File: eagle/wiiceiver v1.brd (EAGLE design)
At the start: 35.2 x 50.8 mm, 16 parts, among them IC1 ATmega328P

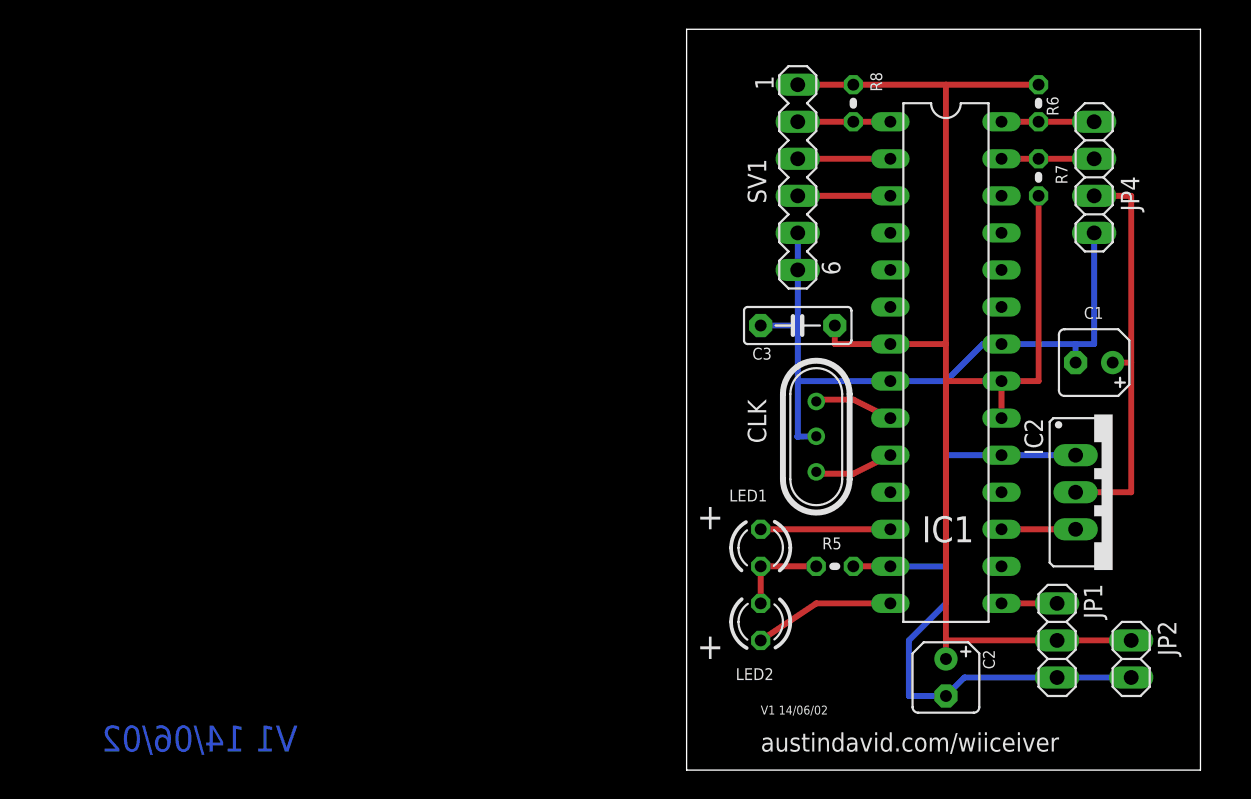
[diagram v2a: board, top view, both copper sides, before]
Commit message: minor update for calibration function
calibrates in 1s now, and more reliably

also some minor changes to the schematic, fixing glitches
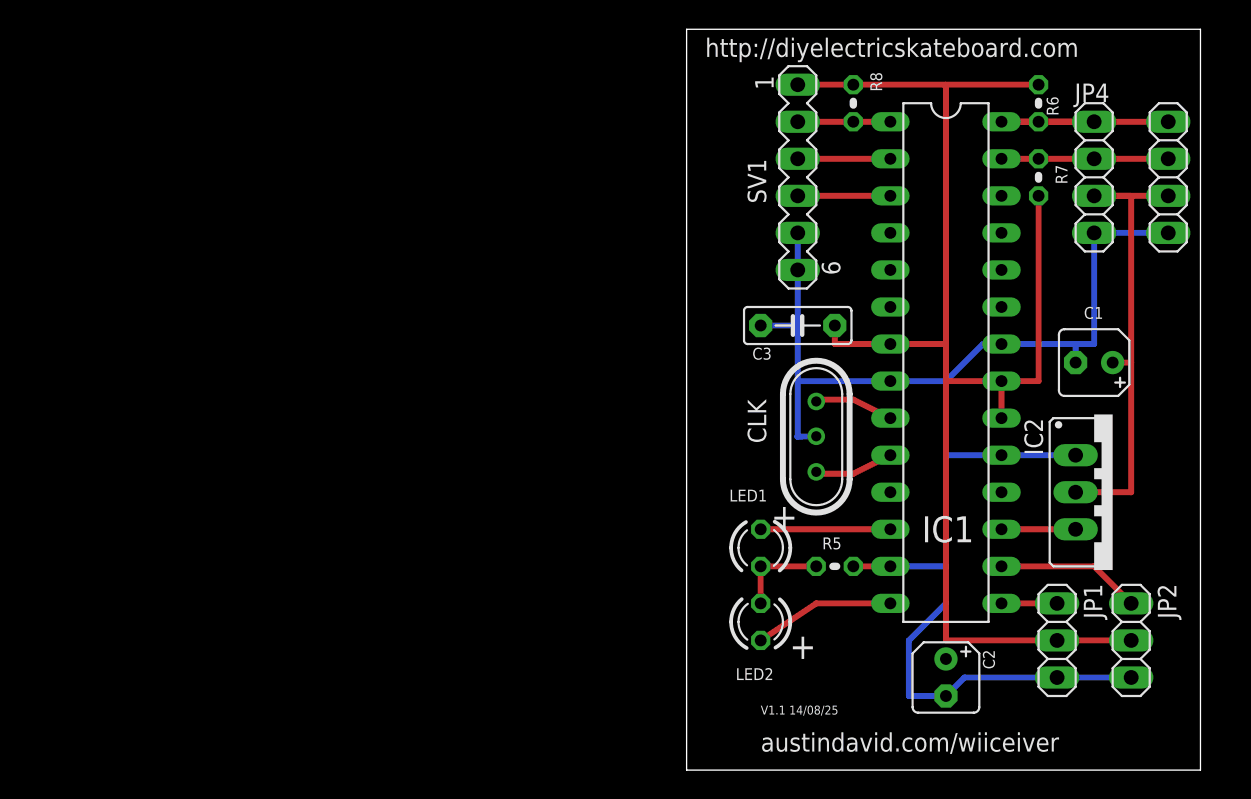
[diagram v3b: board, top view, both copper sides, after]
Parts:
- added JP3: (no value), pinhead:1X04
- JP2: device pinhead:1X02 -> pinhead:1X03
- moved JP2 1.27 mm to (52.1, 30.5)
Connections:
- new net N$3: IC1.26
- new net N$4: IC1.16, JP2.1
- net GND: now also C2.+, JP2.3, JP3.4, R6.2, R7.2, R8.1, SV1.1; no longer JP2.2
- net N$16: now also JP3.2, JP3.3
- net N$21: now also JP3.1
- net VIN: now also JP2.2; no longer C2.+, JP2.1, R6.2, R7.2, R8.1, SV1.1
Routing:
- net GND: track 101.7 -> 136.0 mm
- net VIN: track 99.1 -> 68.6 mm
- net N$21: track 6.35 -> 17.8 mm
- net N$16: track 27.9 -> 38.1 mm
- net N$4: track 0.00 -> 9.94 mm
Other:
- board text added: "V1.1 14/08/25"
- board text added: "http://diyelectricskateboard.com"
- board text removed: "V1 14/06/02"
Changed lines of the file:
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@@
 <setting verticaltext="up"/>
 </settings>
-<grid distance="0.05" unitdist="inch" unit="inch" style="lines" multiple="1" display="yes" altdistance="0.025" altunitdist="inch" altunit="inch"/>
+<grid distance="0.025" unitdist="inch" unit="inch" style="lines" multiple="1" display="yes" altdistance="0.025" altunitdist="inch" altunit="inch"/>
 <layers>
 <layer number="1" name="Top" color="4" fill="1" visible="yes" active="yes"/>
@@
 <wire x1="21.59" y1="72.38" x2="21.59" y2="21.59" width="0" layer="20"/>
 <text x="26.67" y="22.86" size="1.27" layer="25">austindavid.com/wiiceiver</text>
-<text x="24.13" y="29.21" size="1.778" layer="25" rot="MR0">+</text>
-<text x="24.13" y="38.1" size="1.778" layer="25" rot="MR0">+</text>
-<text x="-5.08" y="22.86" size="1.778" layer="16" rot="MR0">V1 14/06/02</text>
-<text x="26.67" y="25.4" size="0.6096" layer="25">V1 14/06/02</text>
+<text x="30.48" y="29.21" size="1.778" layer="25" rot="MR0">+</text>
+<text x="29.21" y="38.1" size="1.778" layer="25" rot="MR0">+</text>
+<text x="26.67" y="25.4" size="0.6096" layer="25">V1.1 14/08/25</text>
+<text x="22.86" y="70.485" size="1.27" layer="25">http://diyelectricskateboard.com</text>
 </plain>
 <attributes>
@@
 </element>
 <element name="JP1" library="pinhead" package="1X03" value="Servo" x="46.99" y="30.48" rot="R270"/>
-<element name="JP2" library="pinhead" package="1X02" value="BEC" x="52.07" y="29.21" rot="R270"/>
+<element name="JP2" library="pinhead" package="1X03" value="BEC" x="52.07" y="30.48" rot="R270"/>
 <element name="CLK" library="crystal" package="HC49U" value="16MHz" x="30.48" y="44.45" smashed="yes" rot="R270">
 <attribute name="OC_NEWARK" value="unknown" x="-11.43" y="25.4" size="1.778" layer="27" rot="R270" display="off"/>
@@
 </element>
 <element name="JP4" library="pinhead" package="1X04" value="Nunchuck Hole" x="49.53" y="62.23" smashed="yes" rot="R270">
-<attribute name="NAME" x="51.3588" y="62.3062" size="1.27" layer="25" ratio="10" rot="R270"/>
+<attribute name="NAME" x="48.1838" y="67.3862" size="1.27" layer="25" ratio="10"/>
 <attribute name="VALUE" x="46.355" y="67.31" size="1.27" layer="27" rot="R270"/>
 </element>
@@
 <attribute name="NAME" x="25.781" y="63.5" size="1.27" layer="25" ratio="10" rot="R270"/>
 <attribute name="VALUE" x="26.289" y="64.77" size="1.27" layer="27" ratio="10" rot="R270"/>
+</element>
+<element name="JP3" library="pinhead" package="1X04" value="" x="54.61" y="62.23" smashed="yes" rot="R270">
+<attribute name="VALUE" x="51.435" y="67.31" size="1.27" layer="27" rot="R270"/>
 </element>
 </elements>
@@
 <contactref element="IC2" pad="2"/>
 <wire x1="48.26" y1="40.64" x2="52.07" y2="40.64" width="0.4064" layer="1"/>
+<contactref element="JP3" pad="3"/>
+<contactref element="JP3" pad="2"/>
+<wire x1="54.61" y1="63.5" x2="49.53" y2="63.5" width="0.4064" layer="1"/>
+<wire x1="49.53" y1="60.96" x2="54.61" y2="60.96" width="0.4064" layer="1"/>
+<wire x1="54.61" y1="60.96" x2="54.61" y2="63.5" width="0" layer="19" extent="1-1"/>
 </signal>
 <signal name="N$21">
@@
 <wire x1="43.18" y1="66.04" x2="45.72" y2="66.04" width="0.4064" layer="1"/>
 <wire x1="45.72" y1="66.04" x2="49.53" y2="66.04" width="0.4064" layer="1"/>
+<contactref element="JP3" pad="1"/>
+<wire x1="43.18" y1="66.04" x2="49.53" y2="66.04" width="0.4064" layer="1"/>
+<wire x1="49.53" y1="66.04" x2="54.61" y2="66.04" width="0.4064" layer="1"/>
 </signal>
 <signal name="N$22">
@@
 <contactref element="R5" pad="2"/>
 <contactref element="JP4" pad="4"/>
-<contactref element="JP2" pad="2"/>
-<contactref element="JP1" pad="3"/>
 <contactref element="C2" pad="-"/>
 <contactref element="IC1" pad="22"/>
@@
 <wire x1="43.18" y1="50.8" x2="48.26" y2="50.8" width="0.4064" layer="16"/>
 <wire x1="48.26" y1="50.8" x2="49.53" y2="50.8" width="0.4064" layer="16"/>
-<wire x1="52.07" y1="27.94" x2="46.99" y2="27.94" width="0.4064" layer="16"/>
 <wire x1="26.67" y1="52.07" x2="29.21" y2="52.07" width="0.4064" layer="16"/>
 <wire x1="29.21" y1="44.45" x2="29.21" y2="48.26" width="0.4064" layer="16"/>
@@
 <wire x1="49.53" y1="58.42" x2="49.53" y2="50.8" width="0.4064" layer="16"/>
 <wire x1="48.26" y1="49.53" x2="48.26" y2="50.8" width="0.4064" layer="16"/>
-<wire x1="46.99" y1="27.94" x2="40.64" y2="27.94" width="0.4064" layer="16"/>
 <wire x1="40.64" y1="27.94" x2="39.37" y2="26.67" width="0.4064" layer="16"/>
 <wire x1="39.37" y1="35.56" x2="39.37" y2="33.02" width="0.4064" layer="16"/>
@@
 <wire x1="29.21" y1="58.42" x2="29.21" y2="55.88" width="0.4064" layer="16"/>
 <wire x1="29.21" y1="55.88" x2="29.21" y2="52.07" width="0.4064" layer="16"/>
+<contactref element="C2" pad="+"/>
+<contactref element="R7" pad="2"/>
+<contactref element="R6" pad="2"/>
+<contactref element="R8" pad="1"/>
+<contactref element="SV1" pad="1"/>
+<contactref element="JP1" pad="3"/>
+<wire x1="33.02" y1="68.58" x2="29.21" y2="68.58" width="0.4064" layer="1"/>
+<contactref element="JP2" pad="3"/>
+<wire x1="52.07" y1="27.94" x2="46.99" y2="27.94" width="0.4064" layer="16"/>
+<wire x1="46.99" y1="27.94" x2="40.64" y2="27.94" width="0.4064" layer="16"/>
+<wire x1="33.02" y1="68.58" x2="45.72" y2="68.58" width="0.4064" layer="1"/>
+<wire x1="45.72" y1="60.96" x2="45.72" y2="48.26" width="0.4064" layer="1"/>
+<contactref element="JP3" pad="4"/>
+<wire x1="54.61" y1="58.42" x2="49.53" y2="58.42" width="0.4064" layer="16"/>
+<wire x1="45.72" y1="60.96" x2="45.72" y2="68.58" width="0" layer="19" extent="1-1"/>
+<wire x1="48.26" y1="49.53" x2="45.72" y2="48.26" width="0" layer="19" extent="1-1"/>
+<wire x1="39.37" y1="29.21" x2="40.64" y2="27.94" width="0" layer="19" extent="16-16"/>
 </signal>
 <signal name="VIN">
-<contactref element="JP2" pad="1"/>
 <contactref element="JP1" pad="2"/>
 <contactref element="IC1" pad="21"/>
@@
 <contactref element="IC1" pad="7"/>
 <contactref element="C3" pad="1"/>
-<contactref element="C2" pad="+"/>
-<contactref element="R7" pad="2"/>
-<contactref element="R6" pad="2"/>
-<contactref element="R8" pad="1"/>
-<wire x1="33.02" y1="68.58" x2="39.37" y2="68.58" width="0.4064" layer="1"/>
 <wire x1="39.37" y1="68.58" x2="39.37" y2="50.8" width="0.4064" layer="1"/>
 <wire x1="39.37" y1="50.8" x2="35.56" y2="50.8" width="0.4064" layer="1"/>
 <wire x1="43.18" y1="45.72" x2="43.18" y2="48.26" width="0.4064" layer="1"/>
-<wire x1="45.72" y1="68.58" x2="39.37" y2="68.58" width="0.4064" layer="1"/>
-<wire x1="46.99" y1="30.48" x2="52.07" y2="30.48" width="0.4064" layer="1"/>
 <wire x1="35.56" y1="50.8" x2="31.75" y2="50.8" width="0.4064" layer="1"/>
 <wire x1="31.75" y1="50.8" x2="31.75" y2="52.07" width="0.4064" layer="1"/>
 <wire x1="43.18" y1="48.26" x2="45.72" y2="48.26" width="0.4064" layer="1"/>
-<wire x1="45.72" y1="48.26" x2="45.72" y2="60.96" width="0.4064" layer="1"/>
 <wire x1="39.37" y1="30.48" x2="46.99" y2="30.48" width="0.4064" layer="1"/>
 <wire x1="39.37" y1="48.26" x2="43.18" y2="48.26" width="0.4064" layer="1"/>
 <wire x1="39.37" y1="30.48" x2="39.37" y2="48.26" width="0.4064" layer="1"/>
 <wire x1="39.37" y1="48.26" x2="39.37" y2="50.8" width="0.4064" layer="1"/>
-<wire x1="39.37" y1="29.21" x2="39.37" y2="30.48" width="0.4064" layer="1"/>
-<contactref element="SV1" pad="1"/>
-<wire x1="33.02" y1="68.58" x2="29.21" y2="68.58" width="0.4064" layer="1"/>
+<contactref element="JP2" pad="2"/>
+<wire x1="52.07" y1="30.48" x2="46.99" y2="30.48" width="0.4064" layer="1"/>
 </signal>
 <signal name="DIP12">
@@
 <wire x1="29.21" y1="66.04" x2="33.02" y2="66.04" width="0.4064" layer="1"/>
 </signal>
+<signal name="N$3">
+<contactref element="IC1" pad="26"/>
+</signal>
+<signal name="N$4">
+<contactref element="JP2" pad="1"/>
+<contactref element="IC1" pad="16"/>
+<wire x1="52.07" y1="33.02" x2="49.53" y2="35.56" width="0.4064" layer="1"/>
+<wire x1="49.53" y1="35.56" x2="43.18" y2="35.56" width="0.4064" layer="1"/>
+</signal>
 </signals>
